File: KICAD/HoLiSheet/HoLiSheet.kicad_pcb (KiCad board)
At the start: 2 copper layers, 20.3 x 25.9 mm, 2 parts, among them J1 Conn_01x06, J2 Conn_01x06

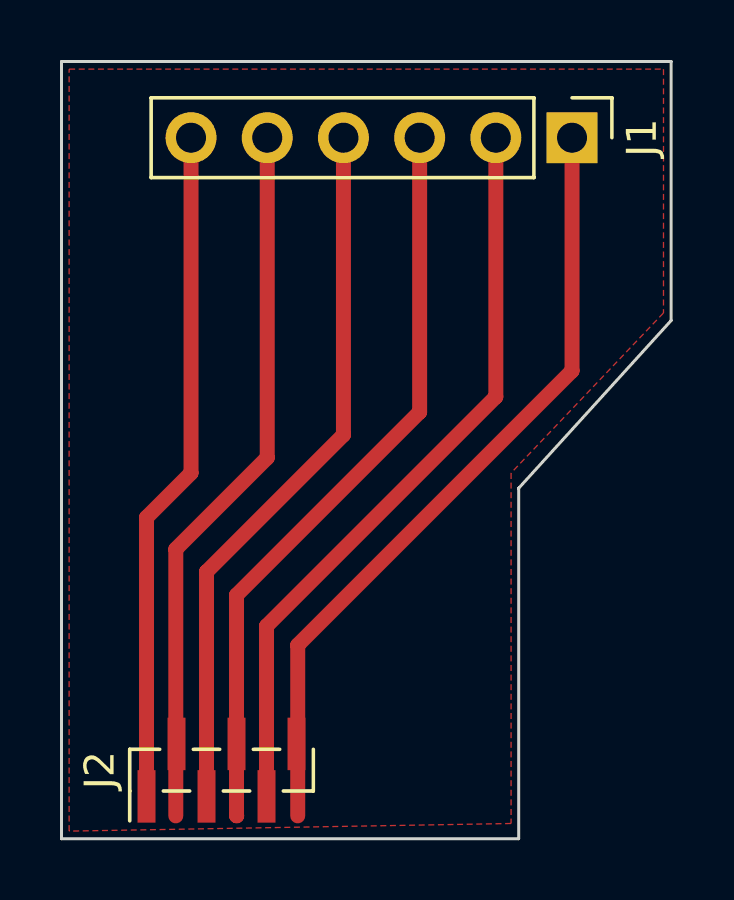
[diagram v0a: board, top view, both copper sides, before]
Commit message: Adding new scanner to the wellplate
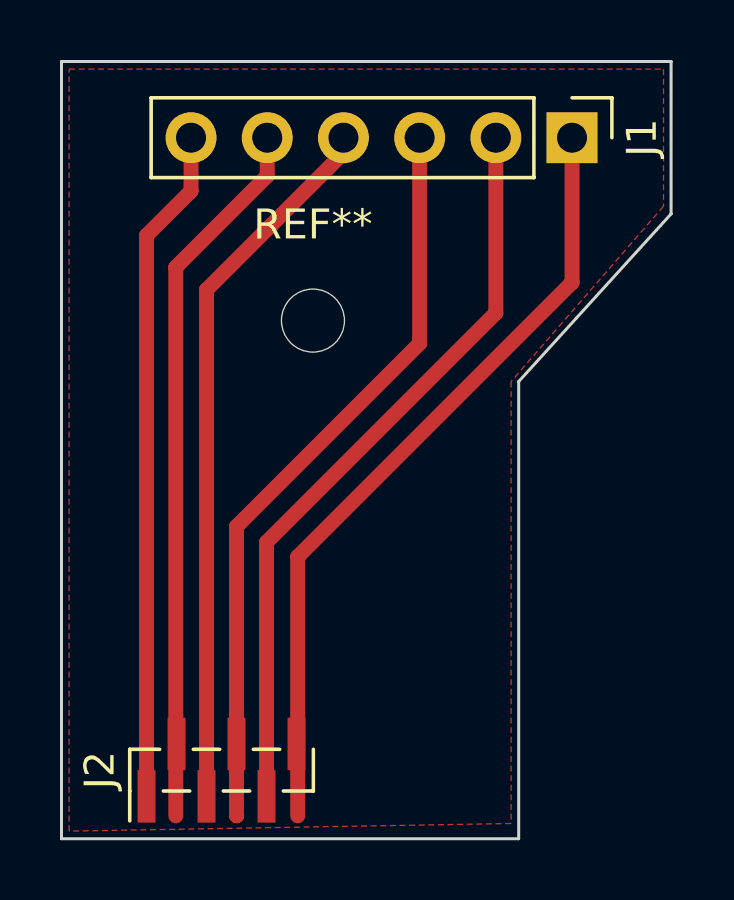
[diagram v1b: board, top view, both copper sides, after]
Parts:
- added REF**: MountingHole_2.1mm, MountingHole:MountingHole_2.1mm, F.Cu at (23.6, 23.9)
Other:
- outline, holes or cut-outs redrawn
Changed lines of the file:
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@@
   (net 5 "Net-(J1-Pad5)")
   (net 6 "Net-(J1-Pad6)")
+  (footprint "MountingHole:MountingHole_2.1mm" (layer "F.Cu")
+    (at 23.622 23.876)
+    (descr "Mounting Hole 2.1mm, no annular")
+    (tags "mounting hole 2.1mm no annular")
+    (attr exclude_from_pos_files exclude_from_bom)
+    (fp_text reference "REF**" (at 0 -3.2) (layer "F.SilkS")
+      (effects (font (size 1 1) (thickness 0.15)))
+    )
+    (fp_text value "MountingHole_2.1mm" (at 0 3.2) (layer "F.Fab")
+      (effects (font (size 1 1) (thickness 0.15)))
+    )
+    (fp_text user "${REFERENCE}" (at 0.3 0) (layer "F.Fab")
+      (effects (font (size 1 1) (thickness 0.15)))
+    )
+    (fp_circle (center 0 0) (end 2.1 0) (layer "Cmts.User") (width 0.15) (fill none))
+    (fp_circle (center 0 0) (end 2.35 0) (layer "F.CrtYd") (width 0.05) (fill none))
+    (pad "" np_thru_hole circle (at 0 0) (size 2.1 2.1) (drill 2.1) (layers *.Cu *.Mask))
+  )
   (footprint "Connector_PinHeader_1.00mm:PinHeader_1x06_P1.00mm_Vertical_SMD_Pin1Left" (layer "F.Cu")
     (at 20.574 38.862 90)
@@
     )
   )
-  (gr_line (start 35.56 23.876) (end 35.56 15.24) (layer "Edge.Cuts") (width 0.1))
+  (gr_line (start 35.56 20.32) (end 35.56 15.24) (layer "Edge.Cuts") (width 0.1))
   (gr_line (start 15.24 41.148) (end 30.48 41.148) (layer "Edge.Cuts") (width 0.1))
   (gr_line (start 35.56 15.24) (end 15.24 15.24) (layer "Edge.Cuts") (width 0.1))
-  (gr_line (start 30.48 41.148) (end 30.48 29.464) (layer "Edge.Cuts") (width 0.1))
+  (gr_line (start 30.48 41.148) (end 30.48 25.908) (layer "Edge.Cuts") (width 0.1))
   (gr_line (start 15.24 15.24) (end 15.24 41.148) (layer "Edge.Cuts") (width 0.1))
-  (gr_line (start 30.48 29.464) (end 35.56 23.876) (layer "Edge.Cuts") (width 0.1))
-  (segment (start 32.258 25.550781) (end 23.114 34.694781) (width 0.5) (layer "F.Cu") (net 1))
-  (segment (start 32.258 17.78) (end 32.258 25.550781) (width 0.5) (layer "F.Cu") (net 1))
-  (segment (start 23.114 34.694781) (end 23.114 40.386) (width 0.5) (layer "F.Cu") (net 1))
-  (segment (start 29.718 26.416) (end 29.718 17.78) (width 0.5) (layer "F.Cu") (net 2))
-  (segment (start 22.074 39.737) (end 22.074 34.06) (width 0.5) (layer "F.Cu") (net 2))
-  (segment (start 22.074 34.06) (end 29.718 26.416) (width 0.5) (layer "F.Cu") (net 2))
+  (gr_line (start 30.48 25.908) (end 35.56 20.32) (layer "Edge.Cuts") (width 0.1))
+  (segment (start 32.258 17.78) (end 32.258 22.606) (width 0.5) (layer "F.Cu") (net 1))
+  (segment (start 32.258 22.606) (end 23.114 31.75) (width 0.5) (layer "F.Cu") (net 1))
+  (segment (start 23.114 31.75) (end 23.114 40.386) (width 0.5) (layer "F.Cu") (net 1))
+  (segment (start 29.718 23.622) (end 29.718 17.78) (width 0.5) (layer "F.Cu") (net 2))
+  (segment (start 22.074 31.266) (end 29.718 23.622) (width 0.5) (layer "F.Cu") (net 2))
+  (segment (start 22.074 39.737) (end 22.074 31.266) (width 0.5) (layer "F.Cu") (net 2))
   (segment (start 21.074 40.378) (end 21.074 37.987) (width 0.5) (layer "F.Cu") (net 3))
   (segment (start 21.074 40.378) (end 21.082 40.386) (width 0.5) (layer "F.Cu") (net 3))
-  (segment (start 27.178 26.924) (end 21.074 33.028) (width 0.5) (layer "F.Cu") (net 3))
-  (segment (start 27.178 17.78) (end 27.178 26.924) (width 0.5) (layer "F.Cu") (net 3))
-  (segment (start 21.074 33.028) (end 21.074 37.987) (width 0.5) (layer "F.Cu") (net 3))
-  (segment (start 20.074 39.737) (end 20.074 32.25) (width 0.5) (layer "F.Cu") (net 4))
-  (segment (start 24.638 27.686) (end 24.638 17.78) (width 0.5) (layer "F.Cu") (net 4))
-  (segment (start 20.074 32.25) (end 24.638 27.686) (width 0.5) (layer "F.Cu") (net 4))
-  (segment (start 19.05 31.496) (end 19.05 40.386) (width 0.5) (layer "F.Cu") (net 5))
-  (segment (start 22.098 17.78) (end 22.098 28.448) (width 0.5) (layer "F.Cu") (net 5))
-  (segment (start 22.098 28.448) (end 19.05 31.496) (width 0.5) (layer "F.Cu") (net 5))
-  (segment (start 18.074 39.737) (end 18.074 30.44) (width 0.5) (layer "F.Cu") (net 6))
-  (segment (start 18.074 30.44) (end 19.558 28.956) (width 0.5) (layer "F.Cu") (net 6))
-  (segment (start 19.558 28.956) (end 19.558 17.78) (width 0.5) (layer "F.Cu") (net 6))
+  (segment (start 27.178 17.78) (end 27.178 24.638) (width 0.5) (layer "F.Cu") (net 3))
+  (segment (start 21.074 30.742) (end 21.074 37.987) (width 0.5) (layer "F.Cu") (net 3))
+  (segment (start 27.178 24.638) (end 21.074 30.742) (width 0.5) (layer "F.Cu") (net 3))
+  (segment (start 24.638 18.288) (end 24.638 17.78) (width 0.5) (layer "F.Cu") (net 4))
+  (segment (start 20.074 39.737) (end 20.074 22.852) (width 0.5) (layer "F.Cu") (net 4))
+  (segment (start 20.074 22.852) (end 24.638 18.288) (width 0.5) (layer "F.Cu") (net 4))
+  (segment (start 22.098 17.78) (end 22.098 19.05) (width 0.5) (layer "F.Cu") (net 5))
+  (segment (start 19.05 22.098) (end 19.05 40.386) (width 0.5) (layer "F.Cu") (net 5))
+  (segment (start 22.098 19.05) (end 19.05 22.098) (width 0.5) (layer "F.Cu") (net 5))
+  (segment (start 18.074 39.737) (end 18.074 21.042) (width 0.5) (layer "F.Cu") (net 6))
+  (segment (start 18.074 21.042) (end 19.558 19.558) (width 0.5) (layer "F.Cu") (net 6))
+  (segment (start 19.558 19.558) (end 19.558 17.78) (width 0.5) (layer "F.Cu") (net 6))
   (zone (net 0) (net_name "") (layer "F.Cu") (hatch edge 0.508)
     (connect_pads (clearance 0.508))
@@
     (polygon
       (pts
-        (xy 35.306 23.622)
-        (xy 30.226 28.956)
+        (xy 35.306 20.066)
+        (xy 30.226 25.908)
         (xy 30.226 40.64)
         (xy 15.494 40.894)
